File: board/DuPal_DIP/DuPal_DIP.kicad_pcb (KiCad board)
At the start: 2 copper layers, 41 parts, among them J1 AVR-ISP-6, J2 RS232, J3 Power IN, SW1 SW_Push, SW2 Power, U1 ATmega8A-PU, U2 74HC595, U3 74HC595, U5 PAL16L8, U6 MAX232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

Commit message: Organized board
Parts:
- moved SW1 155.0 mm to (29.2, 101.6), turned to 90 degrees
- moved D1 151.2 mm to (30.5, 110.5)
- moved R16 144.3 mm to (27.9, 106.7)
- moved C6 142.1 mm to (31.8, 86.4), turned to 90 degrees
- moved C1 141.2 mm to (26.7, 134.6), turned to 90 degrees
- moved C2 132.0 mm to (26.7, 137.2), turned to 270 degrees
- moved R18 131.9 mm to (36.8, 139.7), turned to 90 degrees
- moved C11 126.9 mm to (58.4, 130.8), turned to 270 degrees
- moved Y1 125.9 mm to (31.8, 138.4), turned to 90 degrees
- moved C9 125.9 mm to (47.0, 129.5), turned to 270 degrees
- moved C7 119.5 mm to (53.3, 96.5), turned to 90 degrees
- moved C14 118.7 mm to (45.7, 85.1)
- moved C3 118.3 mm to (61.0, 87.6), turned to 90 degrees
- moved U3 117.6 mm to (54.6, 123.2)
- moved C5 116.7 mm to (45.7, 95.2)
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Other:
- net class POWER added: clearance 0.25, trace_width 0.4, via_dia 0.8, via_drill 0.4

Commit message: DuPAL project
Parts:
- moved C10 6.35 mm to (95.2, 97.8), turned to 270 degrees
- moved U7 5.24 mm to (94.0, 86.4)
- moved D3 5.08 mm to (94.0, 81.3)
- moved C15 4.02 mm to (86.4, 88.9)
- moved D2 2.84 mm to (96.5, 74.9), turned to 180 degrees
- moved C1 2.54 mm to (29.2, 134.6)
- moved C2 2.54 mm to (29.2, 137.2)
- moved R18 2.54 mm to (39.4, 139.7)
- moved Y1 2.54 mm to (34.3, 138.4)
- moved U1 1.27 mm to (43.2, 106.7)
- moved U2 1.27 mm to (55.9, 102.9)
- moved U3 1.27 mm to (55.9, 123.2)
- moved C11 1.27 mm to (59.7, 130.8)
- moved C8 1.27 mm to (59.7, 111.8)
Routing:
- net GND: track 0.00 -> 280.5 mm
- net VCC: track 0.00 -> 197.5 mm
- net /~RESET: track 0.00 -> 106.6 mm
- net Net-(R7-Pad1): track 0.00 -> 80.7 mm
- net /PAL_TRIO2: track 0.00 -> 80.4 mm
- net /PAL_IO5: track 0.00 -> 74.1 mm
- net Net-(R3-Pad1): track 0.00 -> 65.0 mm, vias 0 -> 1
- net /PAL_TRIO1: track 0.00 -> 63.9 mm
- net /PAL_IO4: track 0.00 -> 61.5 mm, vias 0 -> 1
- net Net-(R1-Pad1): track 0.00 -> 59.0 mm
- net /PAL_IO3: track 0.00 -> 56.7 mm
- net /PAL_I10: track 0.00 -> 56.2 mm
- net Net-(R8-Pad1): track 0.00 -> 55.9 mm
- net /PAL_IO6: track 0.00 -> 52.6 mm
- net /PAL_IO2: track 0.00 -> 52.5 mm
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- added copper zone on B.Cu, net GND
- added copper zone on F.Cu, net GND
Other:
- board outline added: 72.4 x 73.7 mm

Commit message: Add logo
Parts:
- added G***: LOGO, logo:logo, F.Cu at (74.9, 101.6)

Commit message: Add front silk text
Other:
- board text added: "7-12V TIP positive"
- board text added: "Activity"
- board text added: "Power LED"
- board text added: "Power Switch"
- board text added: "Put PAL16L8 here"
- board text added: "RESET"
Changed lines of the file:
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@@
   (general
     (thickness 1.6)
-    (drawings 4)
+    (drawings 14)
     (tracks 602)
     (zones 0)
@@
     )
   )
+  (gr_text "Power LED" (at 93.98 72.39) (layer F.SilkS)
+    (effects (font (size 1 1) (thickness 0.15)))
+  )
+  (gr_text Activity (at 38.1 110.49) (layer F.SilkS)
+    (effects (font (size 1 1) (thickness 0.15)))
+  )
+  (gr_text RESET (at 31.75 92.71) (layer F.SilkS)
+    (effects (font (size 1 1) (thickness 0.15)))
+  )
+  (gr_text "7-12V\nTIP positive" (at 71.12 86.36) (layer B.SilkS)
+    (effects (font (size 1 1) (thickness 0.15)) (justify mirror))
+  )
+  (gr_text "Power Switch" (at 85.09 78.74) (layer F.SilkS)
+    (effects (font (size 1 1) (thickness 0.15)))
+  )
+  (gr_line (start 72.39 99.06) (end 71.12 100.33) (layer F.SilkS) (width 0.12))
+  (gr_line (start 69.85 99.06) (end 71.12 100.33) (layer F.SilkS) (width 0.12))
+  (gr_line (start 71.12 100.33) (end 69.85 99.06) (layer F.SilkS) (width 0.12))
+  (gr_line (start 59.69 99.06) (end 72.39 99.06) (layer F.SilkS) (width 0.12))
+  (gr_text "Put PAL16L8 here" (at 66.04 97.79) (layer F.SilkS)
+    (effects (font (size 1 1) (thickness 0.15)))
+  )
   (gr_line (start 99.06 69.85) (end 26.67 69.85) (layer Edge.Cuts) (width 0.05))

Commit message: Add gerbers
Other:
- board text added: "rev.0"
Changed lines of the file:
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@@
   (general
     (thickness 1.6)
-    (drawings 14)
+    (drawings 15)
     (tracks 602)
     (zones 0)
@@
     )
   )
+  (gr_text rev.0 (at 95.25 140.97) (layer F.SilkS)
+    (effects (font (size 1 1) (thickness 0.15)))
+  )
   (gr_text "Power LED" (at 93.98 72.39) (layer F.SilkS)

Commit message: Distance some ICs
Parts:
- moved C8 3.81 mm to (59.7, 108.0)
- moved U2 2.54 mm to (55.9, 100.3)
- moved C3 1.27 mm to (61.0, 86.4)
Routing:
- net /PAL_I10: track 56.2 -> 34.1 mm, vias 0 -> 1
- net Net-(R3-Pad1): track 65.0 -> 45.2 mm, vias 1 -> 0
- net /PAL_IO5: track 74.1 -> 91.8 mm
- net /TTL-RX: track 49.3 -> 34.1 mm
- net Net-(R1-Pad1): track 59.0 -> 44.3 mm
- net /PAL_TRIO2: track 80.4 -> 66.8 mm
- net /PAL_I5: track 37.3 -> 24.5 mm, vias 0 -> 1
- net VCC: track 197.5 -> 210.2 mm
- net /SHFT_SER: track 41.9 -> 53.6 mm
- net /SHFT_RCLK: track 51.3 -> 40.3 mm
- net /PAL_I4: track 33.4 -> 24.2 mm
- net GND: track 280.5 -> 289.0 mm
- net /~SHFT_RESET: track 47.0 -> 38.8 mm
- net /PAL_IO3: track 56.7 -> 63.5 mm
- net /PAL_IO4: track 61.5 -> 54.7 mm
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- added copper zone on F.Cu, net (none)
- removed copper zone on F.Cu, net GND
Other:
- board text added: "rev.1"
- board text removed: "rev.0"

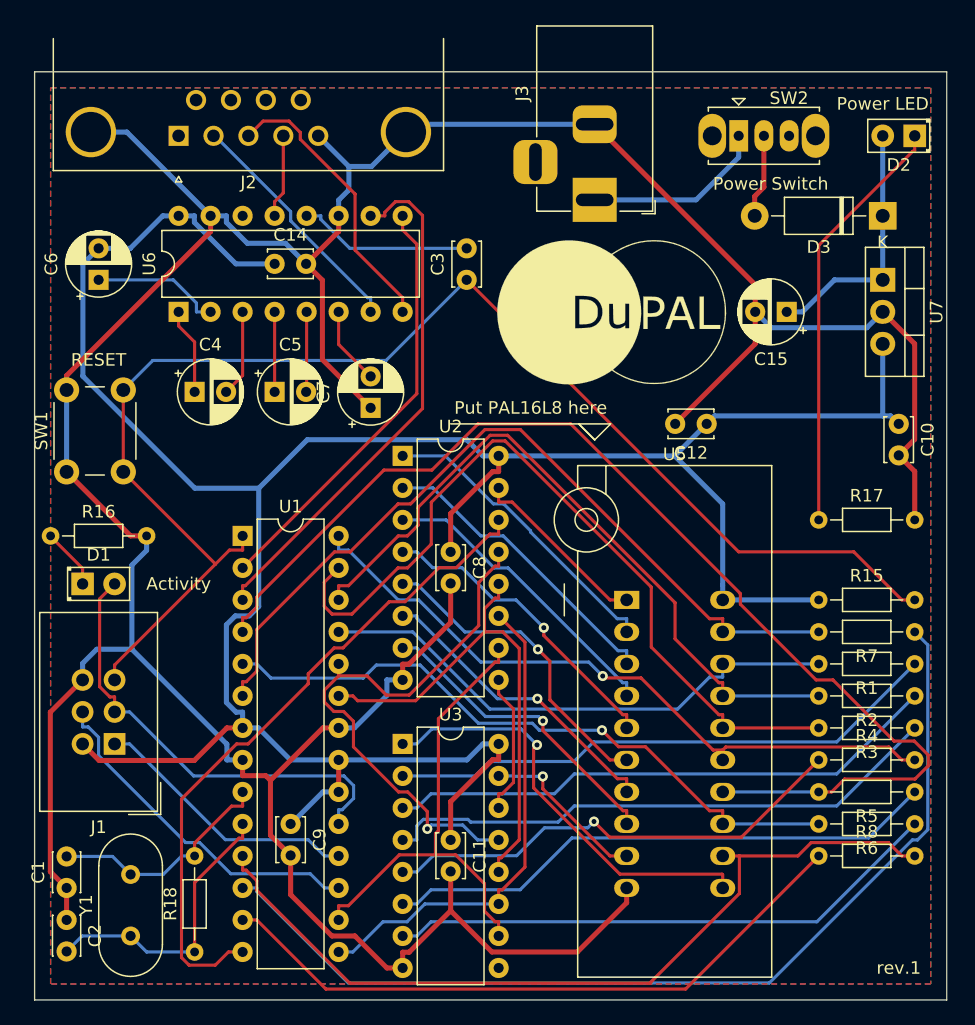
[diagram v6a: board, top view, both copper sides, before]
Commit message: Add rev1.1 board
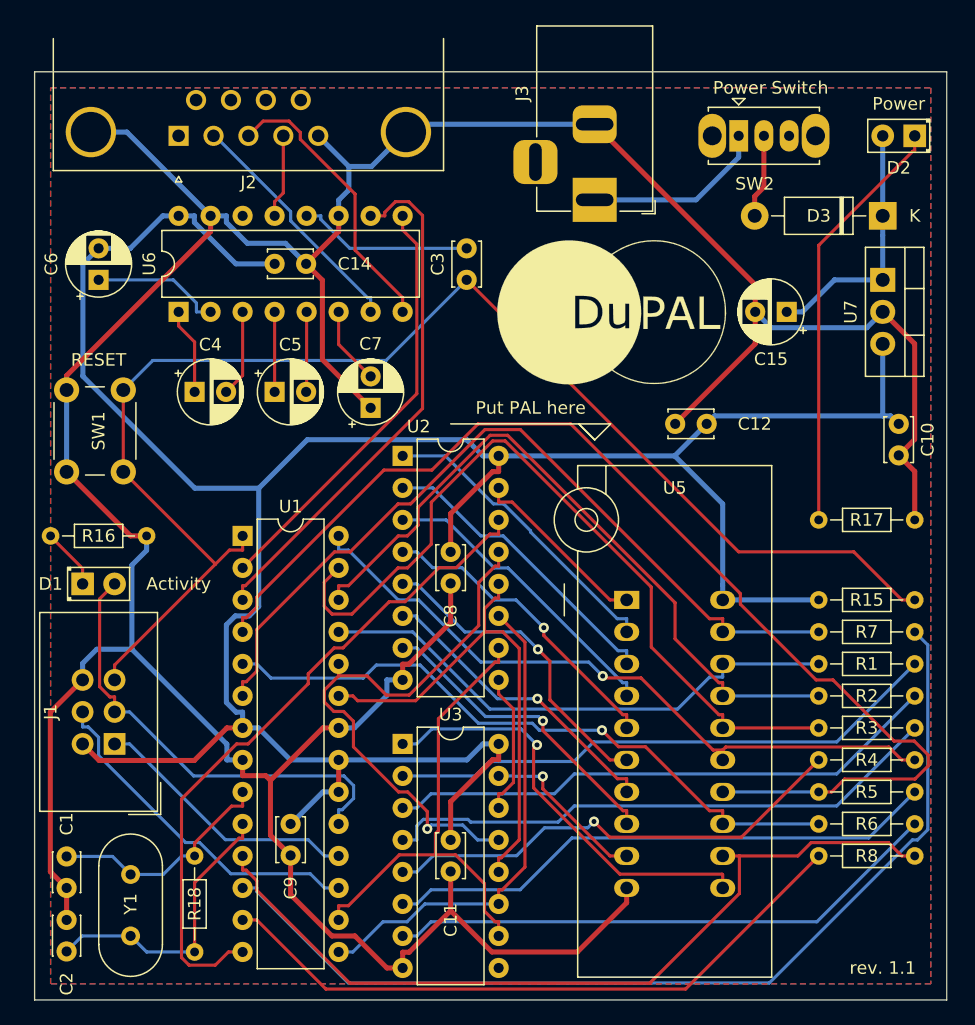
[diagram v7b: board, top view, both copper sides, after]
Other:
- board text added: "Power"
- board text added: "Put PAL here"
- board text added: "rev. 1.1"
- board text removed: "Power LED"
- board text removed: "Put PAL16L8 here"
- board text removed: "rev.1"

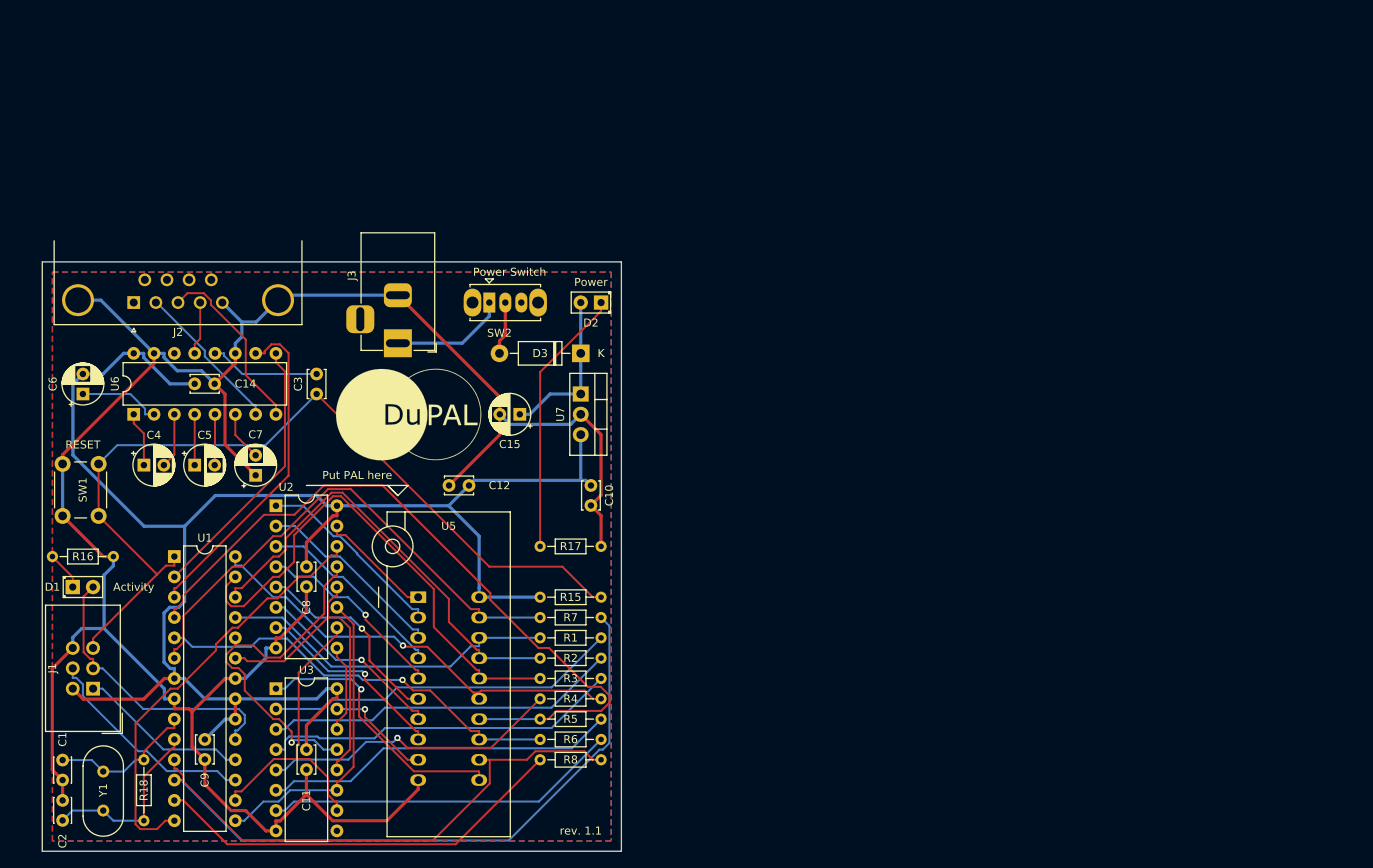
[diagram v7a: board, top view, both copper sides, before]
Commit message: Begin reworking the PCB
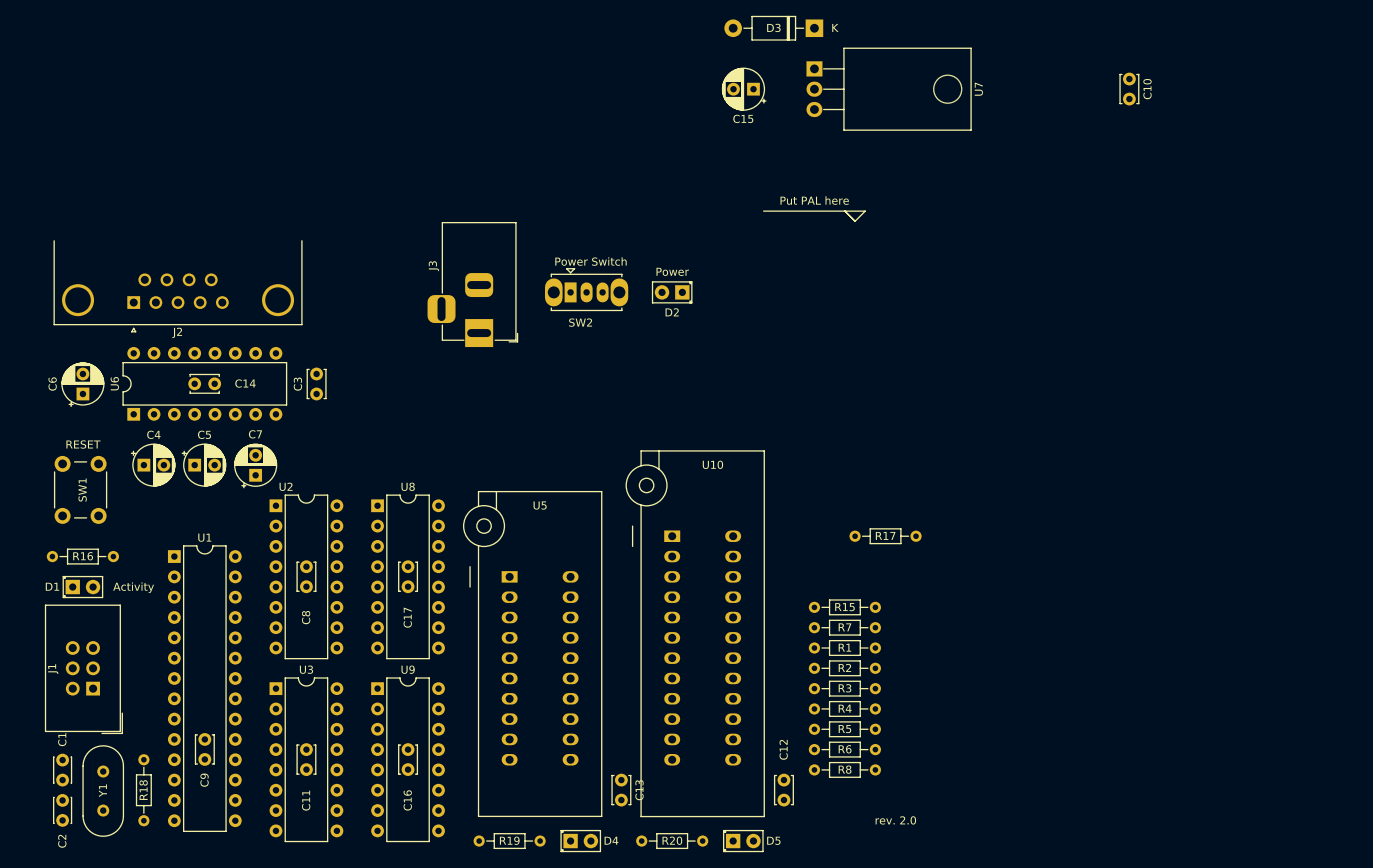
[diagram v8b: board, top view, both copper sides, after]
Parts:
- removed G***: LOGO, logo:logo
- added C13: 100nF, Capacitor_THT:C_Disc_D3.4mm_W2.1mm_P2.50mm, F.Cu at (99.1, 134.6)
- added C16: 100nF, Capacitor_THT:C_Disc_D3.4mm_W2.1mm_P2.50mm, F.Cu at (72.4, 130.8)
- added C17: 100nF, Capacitor_THT:C_Disc_D3.4mm_W2.1mm_P2.50mm, F.Cu at (72.4, 108.0)
- added D4: PAL20_LED, LED_THT:LED_D2.0mm_W4.8mm_H2.5mm_FlatTop, F.Cu at (92.7, 142.2)
- added D5: PAL24_LED, LED_THT:LED_D2.0mm_W4.8mm_H2.5mm_FlatTop, F.Cu at (113.0, 142.2)
- added R19: 680, Resistor_THT:R_Axial_DIN0204_L3.6mm_D1.6mm_P7.62mm_Horizontal, F.Cu at (88.9, 142.2)
- added R20: 680, Resistor_THT:R_Axial_DIN0204_L3.6mm_D1.6mm_P7.62mm_Horizontal, F.Cu at (109.2, 142.2)
- added U10: 24 Pin PAL, Socket:DIP_Socket-24_W4.3_W5.08_W7.62_W10.16_W10.9_3M_224-5248-00-0602J, F.Cu at (105.4, 104.1)
- added U8: 74HC166, Package_DIP:DIP-16_W7.62mm, F.Cu at (68.6, 100.3)
- added U9: 74HC595, Package_DIP:DIP-16_W7.62mm, F.Cu at (68.6, 123.2)
- R16: value 470 -> 680
- U5: value PAL16L8 -> 20 Pin PAL
- U7: footprint Package_TO_SOT_THT:TO-220-3_Vertical -> Package_TO_SOT_THT:TO-220-3_Horizontal_TabDown
- moved C10 84.3 mm to (162.6, 47.0)
- moved C12 53.9 mm to (119.4, 134.6), turned to 270 degrees
- moved C15 50.0 mm to (115.6, 48.3)
- moved D3 50.0 mm to (123.2, 40.6)
- moved U7 50.0 mm to (123.2, 45.7)
- moved R17 39.4 mm to (128.3, 104.1)
- moved R1 34.3 mm to (130.8, 118.1)
- moved R2 34.3 mm to (130.8, 120.7)
- moved R3 34.3 mm to (130.8, 123.2)
- moved R5 34.3 mm to (130.8, 128.3)
- moved R6 34.3 mm to (130.8, 130.8)
- moved R7 34.3 mm to (130.8, 115.6)
- moved R15 34.3 mm to (123.2, 113.0)
- moved R4 34.3 mm to (123.2, 125.7)
- moved R8 34.3 mm to (123.2, 133.3)
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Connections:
- net /SHFT_CLK renamed /SIPO_CLK
- net /SHFT_RCLK renamed /SIPO_RCLK
- net /SHFT_SER renamed /SIPO_SER
- net /~SHFT_OE renamed /~SIPO_OE
- net /~SHFT_RESET renamed /~SIPO_CLR
- J2 pad 1: (no net) -> Net-(J2-Pad1)
- J2 pad 6: (no net) -> Net-(J2-Pad6)
- J2 pad 7: (no net) -> Net-(J2-Pad7)
- J2 pad 8: (no net) -> Net-(J2-Pad8)
- J2 pad 9: (no net) -> Net-(J2-Pad9)
- R1 pad 1: Net-(R1-Pad1) -> /SIPO_O_14
- R1 pad 2: /PAL_IO1 -> /P20_18
- R2 pad 1: Net-(R2-Pad1) -> /SIPO_O_13
- R2 pad 2: /PAL_IO2 -> /P20_17
- R3 pad 1: Net-(R3-Pad1) -> /SIPO_O_12
- R3 pad 2: /PAL_IO3 -> /P20_16
- R4 pad 1: Net-(R4-Pad1) -> /SIPO_O_11
- R4 pad 2: /PAL_IO4 -> /P20_15
- R5 pad 1: Net-(R5-Pad1) -> /SIPO_O_10
- R5 pad 2: /PAL_IO5 -> /P20_14
- R6 pad 1: Net-(R6-Pad1) -> /SIPO_O_9
- R6 pad 2: /PAL_IO6 -> /P20_13
- R7 pad 1: Net-(R7-Pad1) -> /SIPO_O_8
- R7 pad 2: /PAL_TRIO1 -> /P20_19
- R8 pad 1: Net-(R8-Pad1) -> /SIPO_O_7
- R8 pad 2: /PAL_TRIO2 -> /P20_12
- U1 pad 11: /PAL_TRIO2 -> /PISO_CLK
- U1 pad 12: Net-(R7-Pad1) -> /PISO_SER
- U1 pad 13: Net-(R8-Pad1) -> Net-(U1-Pad13)
- U1 pad 25: /PAL_IO1 -> Net-(U1-Pad25)
- U1 pad 26: /PAL_IO2 -> Net-(U1-Pad26)
- U1 pad 27: /PAL_IO3 -> Net-(D4-Pad2)
- U1 pad 28: /PAL_IO4 -> Net-(D5-Pad2)
- U1 pad 4: /PAL_IO5 -> /~PISO_CLR
- U1 pad 5: /PAL_IO6 -> /PISO_SH
- U1 pad 6: /PAL_TRIO1 -> /PISO_INH
- U2 pad 1: /PAL_I2 -> /SIPO_O_2
- U2 pad 15: /PAL_I1 -> /SIPO_O_1
- U2 pad 2: /PAL_I3 -> /P24_23
- U2 pad 3: /PAL_I4 -> /P24_14
- U2 pad 4: /PAL_I5 -> /P24_13
- U2 pad 5: /PAL_I6 -> /P24_11
- U2 pad 6: /PAL_I7 -> /SIPO_O_7
- U2 pad 7: /PAL_I8 -> /SIPO_O_8
- U3 pad 1: /PAL_I10 -> /SIPO_O_10
- U3 pad 15: /PAL_I9 -> /SIPO_O_9
- U3 pad 2: Net-(R1-Pad1) -> /SIPO_O_11
- U3 pad 3: Net-(R2-Pad1) -> /SIPO_O_12
- U3 pad 4: Net-(R3-Pad1) -> /SIPO_O_13
- U3 pad 5: Net-(R4-Pad1) -> /SIPO_O_14
- U3 pad 6: Net-(R5-Pad1) -> /P20_11
- U3 pad 7: Net-(R6-Pad1) -> /P20_9
- U3 pad 9: (no net) -> Net-(U3-Pad9)
- U5 pad 1: /PAL_I1 -> /P20_1
- U5 pad 11: /PAL_I10 -> /P20_11
- U5 pad 12: /PAL_TRIO2 -> /P20_12
- U5 pad 13: /PAL_IO6 -> /P20_13
- U5 pad 14: /PAL_IO5 -> /P20_14
- U5 pad 15: /PAL_IO4 -> /P20_15
- U5 pad 16: /PAL_IO3 -> /P20_16
- U5 pad 17: /PAL_IO2 -> /P20_17
- U5 pad 18: /PAL_IO1 -> /P20_18
- U5 pad 19: /PAL_TRIO1 -> /P20_19
- U5 pad 2: /PAL_I2 -> /P20_2
- U5 pad 3: /PAL_I3 -> /P20_3
- U5 pad 4: /PAL_I4 -> /P20_4
- U5 pad 5: /PAL_I5 -> /P20_5
- U5 pad 6: /PAL_I6 -> /P20_6
- U5 pad 7: /PAL_I7 -> /P20_7
- U5 pad 8: /PAL_I8 -> /P20_8
- U5 pad 9: /PAL_I9 -> /P20_9
- U6 pad 14: (no net) -> Net-(U6-Pad14)
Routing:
- net GND: track 289.0 -> 0.00 mm
- net VCC: track 210.2 -> 0.00 mm
- net /~RESET: track 110.0 -> 0.00 mm
- net /PAL_IO5: track 91.8 -> 0.00 mm
- net Net-(R7-Pad1): track 78.8 -> 0.00 mm
- net /PAL_TRIO2: track 66.8 -> 0.00 mm
- net /PAL_TRIO1: track 64.3 -> 0.00 mm
- net /PAL_IO3: track 63.5 -> 0.00 mm
- net /PAL_IO2: track 55.9 -> 0.00 mm
- net /PAL_IO4: track 54.7 -> 0.00 mm, vias 1 -> 0
- net /SIPO_SER: track 53.6 -> 0.00 mm
- net /PAL_IO6: track 52.5 -> 0.00 mm, vias 1 -> 0
- net Net-(R8-Pad1): track 52.4 -> 0.00 mm
- net Net-(R3-Pad1): track 45.2 -> 0.00 mm
- net /~SIPO_OE: track 44.8 -> 0.00 mm, vias 1 -> 0
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- removed copper zone on F.Cu, net (none)
- removed copper zone on B.Cu, net GND
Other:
- board outline removed
- board text added: "rev. 2.0"
- board text removed: "rev. 1.1"
